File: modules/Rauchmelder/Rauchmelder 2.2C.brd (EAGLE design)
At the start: 38 x 65 mm, 49 parts, among them IC1 MC34063AD, IC3 LPC922FDH, Q1 BC856, Q3 BCP52, T1 BC848

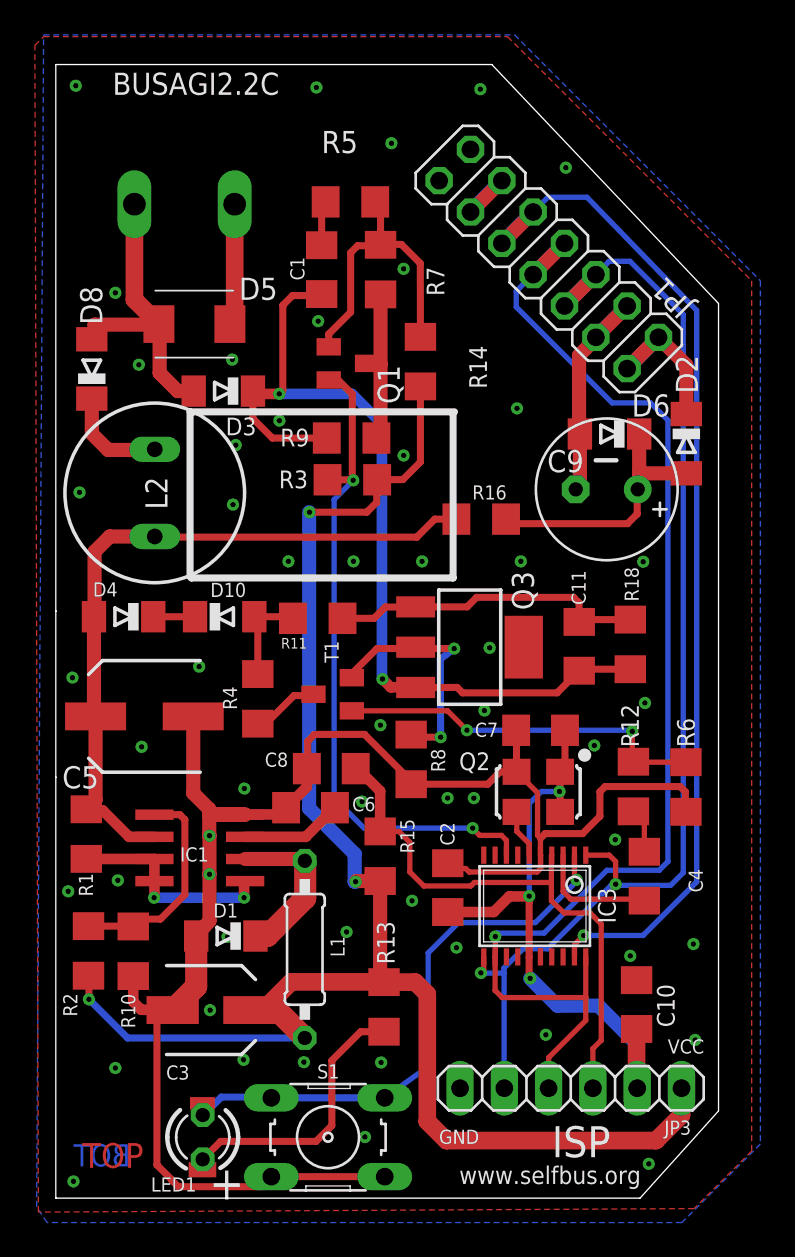
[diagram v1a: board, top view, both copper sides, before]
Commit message: kosmetik am silk
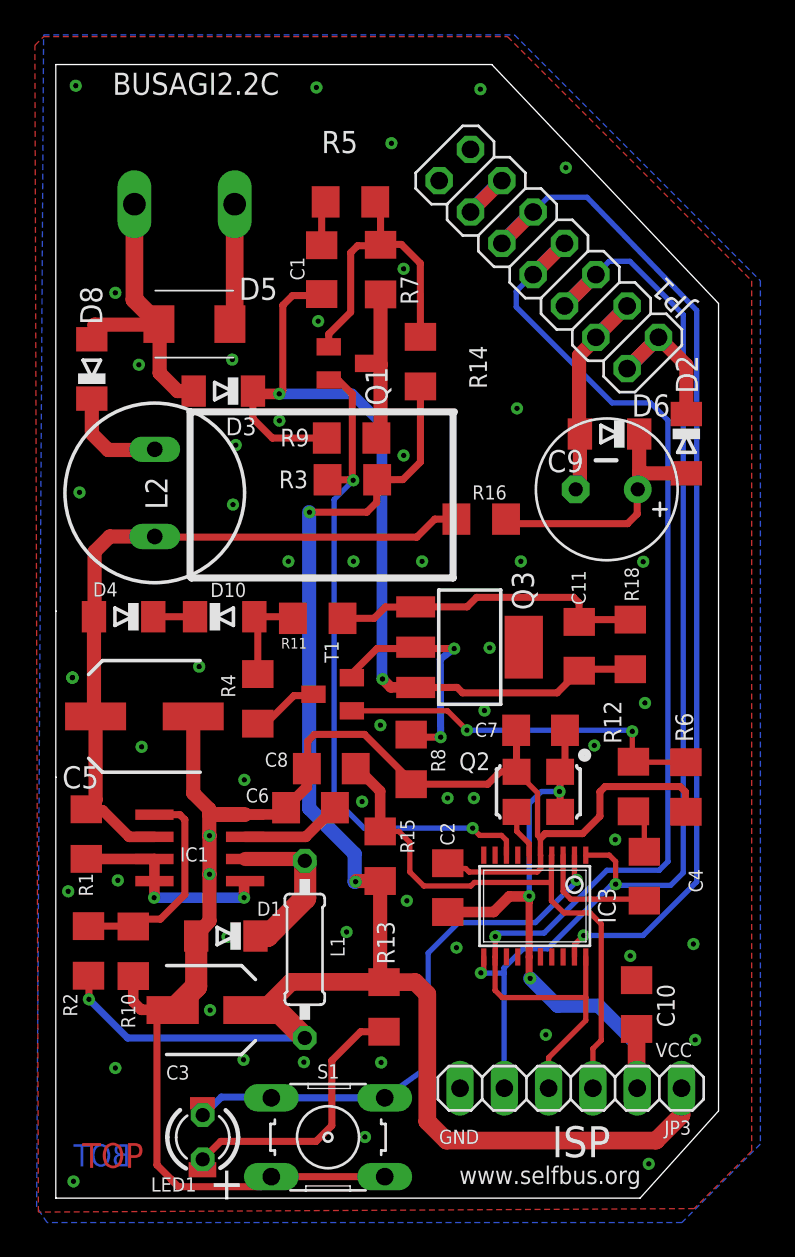
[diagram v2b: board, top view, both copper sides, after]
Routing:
- net GND: vias 54 -> 55
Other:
- board text added: "35V"
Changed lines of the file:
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@@
 <layer number="24" name="bOrigins" color="15" fill="1" visible="yes" active="yes"/>
 <layer number="25" name="tNames" color="7" fill="1" visible="yes" active="yes"/>
-<layer number="26" name="bNames" color="7" fill="1" visible="no" active="yes"/>
+<layer number="26" name="bNames" color="7" fill="1" visible="yes" active="yes"/>
 <layer number="27" name="tValues" color="7" fill="1" visible="yes" active="yes"/>
-<layer number="28" name="bValues" color="7" fill="1" visible="no" active="yes"/>
+<layer number="28" name="bValues" color="7" fill="1" visible="yes" active="yes"/>
 <layer number="29" name="tStop" color="7" fill="3" visible="no" active="yes"/>
 <layer number="30" name="bStop" color="7" fill="6" visible="no" active="yes"/>
@@
 <text x="31.80875" y="4.124425" size="1.778" layer="25" rot="R180">ISP</text>
 <text x="24.274325" y="3.92245" size="0.8128" layer="25" rot="R180">GND</text>
-<text x="37.174375" y="9.10245" size="0.8128" layer="25" rot="R180">VCC</text>
+<text x="36.474375" y="8.90245" size="0.8128" layer="25" rot="R180">VCC</text>
 <text x="33.545625" y="1.825625" size="1.016" layer="25" rot="R180">www.selfbus.org</text>
 <text x="3.254375" y="63.2619" size="1.27" layer="21" font="vector" ratio="10">BUSAGI2.2C</text>
@@
 <wire x1="30.95625" y1="42.306875" x2="32.146875" y2="42.306875" width="0.254" layer="21"/>
 <circle x="30.32125" y="25.4" radius="0.1774875" width="0.4064" layer="21"/>
+<text x="3.7" y="25.5" size="1.016" layer="27">35V</text>
+<text x="7.6" y="11.7" size="1.016" layer="27">16V</text>
 </plain>
 <attributes>
@@
 </element>
 <element name="R6" library="rcl" package="R1206" value="100k" x="36.132975" y="23.574175" smashed="yes" rot="R90">
-<attribute name="NAME" x="36.639525" y="25.864725" size="1.016" layer="25" ratio="10" rot="R90"/>
+<attribute name="NAME" x="36.539525" y="26.164725" size="1.016" layer="25" ratio="10" rot="R90"/>
 <attribute name="VALUE" x="35.11385" y="22.253375" size="0.8128" layer="27" ratio="10" rot="R90"/>
 </element>
@@
 <element name="R2" library="rcl" package="R1206" value="3k6" x="1.874425" y="14.175525" smashed="yes" rot="R270">
 <attribute name="NAME" x="1.234925" y="10.411025" size="0.8128" layer="25" ratio="10" rot="R90"/>
-<attribute name="VALUE" x="1.67775" y="11.91195" size="1.27" layer="27" ratio="10" rot="R270"/>
+<attribute name="VALUE" x="1.47775" y="11.21195" size="1.27" layer="27" ratio="10" rot="R270"/>
 </element>
 <element name="R10" library="rcl" package="R1206" value="2k2" x="4.440625" y="14.1553" smashed="yes" rot="R90">
@@
 <element name="C3" library="rcl" package="SANYO-OSCON_SMD_B6" value="100µ" x="8.899725" y="10.784425" smashed="yes">
 <attribute name="NAME" x="7.664325" y="7.6086" size="0.8128" layer="25" ratio="10" rot="R180"/>
-<attribute name="VALUE" x="7.921225" y="9.271275" size="0.8128" layer="27" ratio="10"/>
+<attribute name="VALUE" x="7.721225" y="8.971275" size="0.8128" layer="27" ratio="10"/>
 </element>
 <element name="C6" library="rcl" package="C1206" value="470p" x="14.603925" y="22.387425" smashed="yes" rot="R180">
-<attribute name="NAME" x="18.3282" y="22.998425" size="0.8128" layer="25" ratio="10" rot="R180"/>
+<attribute name="NAME" x="12.2282" y="23.498425" size="0.8128" layer="25" ratio="10" rot="R180"/>
 <attribute name="VALUE" x="15.3438" y="21.37565" size="0.8128" layer="27" ratio="10" rot="R180"/>
 </element>
 <element name="R4" library="rcl" package="R1206" value="2k2" x="11.5821" y="28.628575" smashed="yes" rot="R90">
-<attribute name="NAME" x="10.39185" y="28.000975" size="0.8128" layer="25" ratio="10" rot="R90"/>
-<attribute name="VALUE" x="13.5616" y="27.8807" size="1.016" layer="27" ratio="10" rot="R90"/>
+<attribute name="NAME" x="10.29185" y="28.700975" size="0.8128" layer="25" ratio="10" rot="R90"/>
+<attribute name="VALUE" x="13.7616" y="27.6807" size="1.016" layer="27" ratio="10" rot="R90"/>
 </element>
 <element name="R11" library="rcl" package="R1206" value="1k" x="15.016825" y="33.245775" smashed="yes" rot="R180">
@@
 </element>
 <element name="R7" library="rcl" package="R1206" value="47k" x="18.620075" y="53.240075" smashed="yes" rot="R90">
-<attribute name="NAME" x="22.279375" y="51.731875" size="1.016" layer="25" ratio="10" rot="R90"/>
-<attribute name="VALUE" x="21.06325" y="51.836575" size="1.27" layer="27" ratio="10" rot="R90"/>
+<attribute name="NAME" x="20.779375" y="51.231875" size="1.016" layer="25" ratio="10" rot="R90"/>
+<attribute name="VALUE" x="22.26325" y="51.836575" size="1.27" layer="27" ratio="10" rot="R90"/>
 </element>
 <element name="R8" library="rcl" package="R1206" value="5R6" x="20.3756" y="25.1568" smashed="yes" rot="R90">
@@
 </element>
 <element name="R12" library="rcl" package="R1206" value="5k6" x="33.12125" y="23.6" smashed="yes" rot="R90">
-<attribute name="NAME" x="33.4318" y="25.8556" size="1.016" layer="25" ratio="10" rot="R90"/>
+<attribute name="NAME" x="32.4318" y="26.0556" size="1.016" layer="25" ratio="10" rot="R90"/>
 <attribute name="VALUE" x="32.013175" y="21.949" size="1.27" layer="27" ratio="10" rot="R90"/>
 </element>
@@
 <element name="IC3" library="LPCGira" package="TSSOP20" value="LPC922FDH" x="27.46375" y="16.748125" smashed="yes" rot="R180">
 <attribute name="NAME" x="31.088725" y="17.79905" size="1.016" layer="25" ratio="10" rot="R270"/>
-<attribute name="VALUE" x="23.1872" y="11.83255" size="1.016" layer="27" ratio="10"/>
+<attribute name="VALUE" x="22.1872" y="11.03255" size="1.016" layer="27" ratio="10"/>
 </element>
 <element name="IC1" library="mc34063" package="SOIC8" value="MC34063AD" x="8.255" y="20.081875" smashed="yes" rot="R90">
 <attribute name="NAME" x="8.76" y="20.114875" size="0.8128" layer="25" rot="R180"/>
-<attribute name="VALUE" x="12.79375" y="24.218875" size="1.27" layer="27" rot="R180"/>
+<attribute name="VALUE" x="9.99375" y="23.618875" size="0.8128" layer="27" rot="R180"/>
 </element>
 <element name="U$1" library="con-wago" package="BUSKLEMME243-724" value="EIB" x="7.381875" y="56.99125" rot="R180"/>
 <element name="D1" library="diode" package="MINIMELF" value="BAT46" x="9.749375" y="15.03" smashed="yes" rot="R180">
-<attribute name="NAME" x="10.44475" y="16.900125" size="0.8128" layer="25" rot="R180"/>
-<attribute name="VALUE" x="11.82575" y="16.711625" size="0.8128" layer="27" rot="R270"/>
+<attribute name="NAME" x="12.94475" y="17.000125" size="0.8128" layer="25" rot="R180"/>
+<attribute name="VALUE" x="7.188375" y="16.12575" size="0.8128" layer="27"/>
 </element>
 <element name="D2" library="diode" package="MINIMELF" value="BAT46" x="36.15375" y="43.259375" smashed="yes" rot="R270">
@@
 </element>
 <element name="Q1" library="transistor-pnp" package="SOT23-BEC" value="BC856" x="16.748125" y="47.863125" smashed="yes" rot="R270">
-<attribute name="NAME" x="18.453125" y="47.768125" size="1.27" layer="25" rot="R270"/>
-<attribute name="VALUE" x="13.431875" y="50.7175" size="1.27" layer="27" rot="R270"/>
+<attribute name="NAME" x="17.753125" y="47.668125" size="1.27" layer="25" rot="R270"/>
+<attribute name="VALUE" x="13.331875" y="51.1175" size="1.27" layer="27" rot="R270"/>
 </element>
 <element name="T1" library="transistor" package="SOT23" value="BC848" x="15.875" y="28.8925" smashed="yes" rot="R90">
@@
 <element name="C10" library="rcl" package="C1206" value="1µ" x="33.3" y="11.1" smashed="yes" rot="R270">
 <attribute name="NAME" x="34.47" y="12.27" size="1.016" layer="25" rot="R270"/>
-<attribute name="VALUE" x="30.96" y="10.67" size="1.016" layer="27" rot="R270"/>
+<attribute name="VALUE" x="30.96" y="12.17" size="1.016" layer="27" rot="R270"/>
 </element>
 </elements>
@@
 <via x="14.225625" y="7.79625" extent="1-16" drill="0.3"/>
 <via x="18.653125" y="7.77875" extent="1-16" drill="0.3"/>
-<via x="20.42625" y="17.05125" extent="1-16" drill="0.3"/>
+<via x="20.12625" y="17.05125" extent="1-16" drill="0.3"/>
 <via x="18.613125" y="27.12" extent="1-16" drill="0.3"/>
 <via x="32.940625" y="13.890625" extent="1-16" drill="0.3"/>
@@
 <via x="10.11875" y="48.08" extent="1-16" drill="0.3"/>
 <via x="8.22125" y="30.47625" extent="1-16" drill="0.3"/>
-<via x="10.810625" y="23.481875" extent="1-16" drill="0.3"/>
+<via x="10.810625" y="23.981875" extent="1-16" drill="0.3"/>
 <wire x1="10.855" y1="21.986875" x2="10.868125" y2="22" width="0.6096" layer="1"/>
 <wire x1="10.868125" y1="22" x2="13" y2="22" width="0.6096" layer="1"/>
@@
 <via x="32.076875" y="20.555625" extent="1-16" drill="0.3"/>
 <via x="17.563125" y="22.739375" extent="1-16" drill="0.3"/>
+<via x="0.9525" y="29.845" extent="1-16" drill="0.3"/>
 </signal>
 <signal name="VCC">

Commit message: Passmarken-vias zugefügt
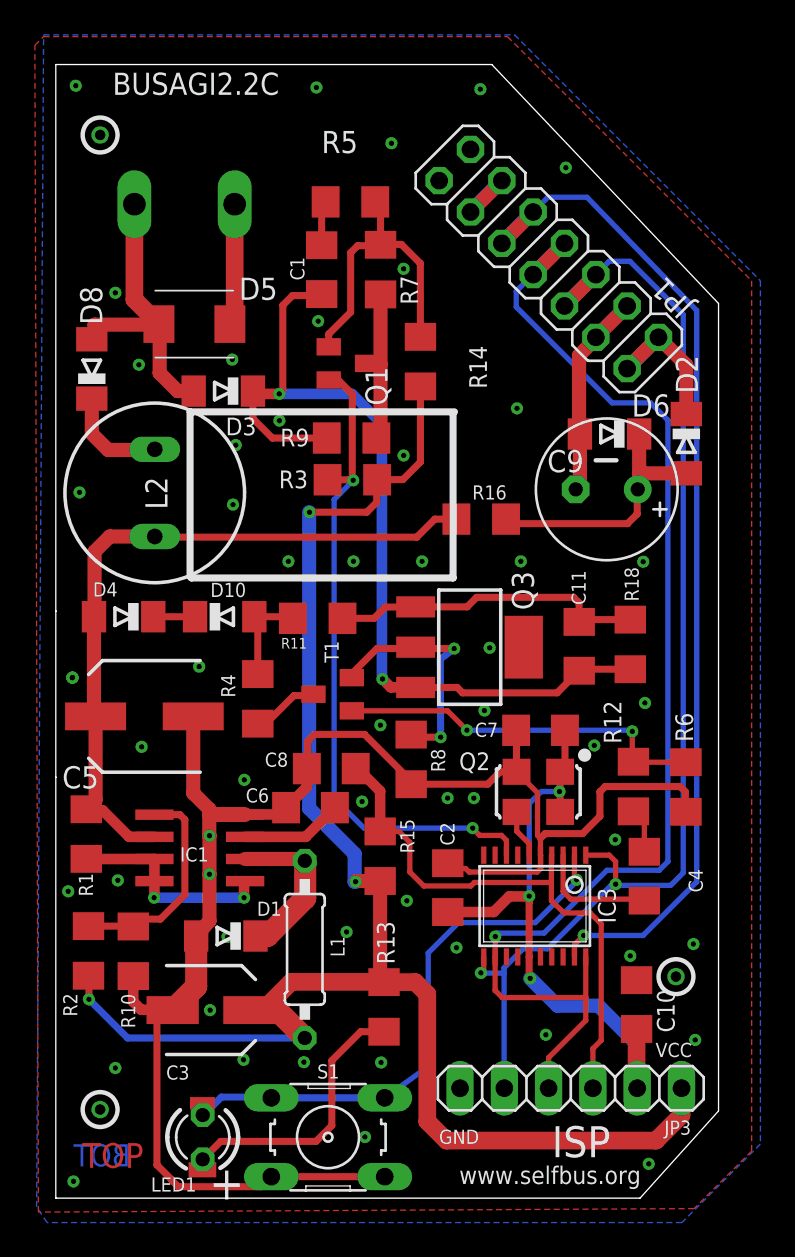
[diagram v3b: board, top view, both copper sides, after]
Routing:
- net GND: vias 55 -> 58
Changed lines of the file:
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@@
 <setting verticaltext="up"/>
 </settings>
-<grid distance="0.1" unitdist="mm" unit="mm" style="lines" multiple="1" display="yes" altdistance="6.25" altunitdist="mil" altunit="mil"/>
+<grid distance="3.93700787" unitdist="mil" unit="mil" style="lines" multiple="1" display="yes" altdistance="6.25" altunitdist="mil" altunit="mil"/>
 <layers>
 <layer number="1" name="Top" color="4" fill="1" visible="yes" active="yes"/>
@@
 <text x="3.7" y="25.5" size="1.016" layer="27">35V</text>
 <text x="7.6" y="11.7" size="1.016" layer="27">16V</text>
+<circle x="2.54" y="60.96" radius="1" width="0.254" layer="21"/>
+<circle x="2.54" y="5.08" radius="1" width="0.254" layer="21"/>
+<circle x="35.56" y="12.7" radius="1" width="0.254" layer="21"/>
 </plain>
 <attributes>
@@
 </element>
 <element name="C10" library="rcl" package="C1206" value="1µ" x="33.3" y="11.1" smashed="yes" rot="R270">
-<attribute name="NAME" x="34.47" y="12.27" size="1.016" layer="25" rot="R270"/>
+<attribute name="NAME" x="34.47" y="11.97" size="1.016" layer="25" rot="R270"/>
 <attribute name="VALUE" x="30.96" y="12.17" size="1.016" layer="27" rot="R270"/>
 </element>
@@
 <via x="17.563125" y="22.739375" extent="1-16" drill="0.3"/>
 <via x="0.9525" y="29.845" extent="1-16" drill="0.3"/>
+<via x="35.56" y="12.7" extent="1-16" drill="0.6" shape="square"/>
+<via x="2.54" y="60.96" extent="1-16" drill="0.6" shape="square"/>
+<via x="2.54" y="5.08" extent="1-16" drill="0.6" shape="square"/>
 </signal>
 <signal name="VCC">
